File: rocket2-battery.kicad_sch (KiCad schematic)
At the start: 57 parts, among them J1 Conn_01x07, J2 SMA, J3 ARM Cortex Debug, P1 PAD_SMD, P2 PAD_SMD, P3 PAD_SMD, P4 PAD_SMD, P5 PAD_SMD, P6 PAD_SMD, Q1 NMOS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

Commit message: some minor fixes
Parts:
- added D17, D18: 30V 2A, Diode_SMD:D_0603_1608Metric_Pad1.05x0.95mm_HandSolder, symbol Device:D_Schottky
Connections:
- net +24V: now also D18.2 (A)
- net BATT_MAIN+: now also D17.2 (A); no longer C1.1, U1.1 (IN)
- new net: C1.1, D17.1 (K), D18.1 (K), U1.1 (IN)
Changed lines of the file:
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@@
   (junction (at 252.73 123.19) (diameter 0) (color 0 0 0 0)
   )
-  (junction (at 142.24 158.75) (diameter 0) (color 0 0 0 0)
-  )
   (junction (at 168.91 123.19) (diameter 0) (color 0 0 0 0)
   )
@@
   (junction (at 187.96 25.4) (diameter 0) (color 0 0 0 0)
   )
+  (junction (at 142.24 158.75) (diameter 0) (color 0 0 0 0)
+  )
   (junction (at 241.3 44.45) (diameter 0) (color 0 0 0 0)
   )
@@
   (junction (at 86.36 92.71) (diameter 0) (color 0 0 0 0)
   )
+  (junction (at 142.24 153.67) (diameter 0) (color 0 0 0 0)
+  )
   (junction (at 74.93 115.57) (diameter 0) (color 0 0 0 0)
   )
@@
     (stroke (width 0) (type default))
   )
+  (wire (pts (xy 153.67 149.86) (xy 151.13 149.86))
+    (stroke (width 0) (type default))
+  )
   (wire (pts (xy 151.13 129.54) (xy 151.13 132.08))
     (stroke (width 0) (type default))
@@
     (stroke (width 0) (type default))
   )
+  (wire (pts (xy 142.24 153.67) (xy 146.05 153.67))
+    (stroke (width 0) (type default))
+  )
   (wire (pts (xy 185.42 95.25) (xy 185.42 96.52))
     (stroke (width 0) (type default))
@@
     (stroke (width 0) (type default))
   )
+  (wire (pts (xy 142.24 149.86) (xy 142.24 153.67))
+    (stroke (width 0) (type default))
+  )
   (wire (pts (xy 185.42 25.4) (xy 187.96 25.4))
     (stroke (width 0) (type default))
@@
     (stroke (width 0) (type default))
   )
+  (wire (pts (xy 143.51 149.86) (xy 142.24 149.86))
+    (stroke (width 0) (type default))
+  )
   (wire (pts (xy 241.3 44.45) (xy 241.3 49.53))
     (stroke (width 0) (type default))
@@
     (stroke (width 0) (type default))
   )
+  (wire (pts (xy 142.24 153.67) (xy 142.24 158.75))
+    (stroke (width 0) (type default))
+  )
   (wire (pts (xy 31.75 60.96) (xy 31.75 83.82))
     (stroke (width 0) (type default))
@@
     (stroke (width 0) (type default))
   )
-  (wire (pts (xy 135.89 158.75) (xy 142.24 158.75))
-    (stroke (width 0) (type default))
-  )
   (wire (pts (xy 200.66 156.21) (xy 203.2 156.21))
     (stroke (width 0) (type default))
@@
     (stroke (width 0) (type default))
   )
+  (wire (pts (xy 156.21 153.67) (xy 153.67 153.67))
+    (stroke (width 0) (type default))
+  )
   (wire (pts (xy 184.15 123.19) (xy 184.15 124.46))
     (stroke (width 0) (type default))
@@
     (effects (font (size 1.27 1.27)) (justify left bottom))
   )
-  (label "BATT_MAIN+" (at 135.89 158.75 0) (fields_autoplaced)
+  (label "BATT_MAIN+" (at 156.21 153.67 0) (fields_autoplaced)
     (effects (font (size 1.27 1.27)) (justify left bottom))
   )
@@
   )
   (symbol (lib_id "UCIRP-KiCAD-Lib:NCV8730") (at 157.48 161.29 0) (unit 1)
-    (in_bom yes) (on_board yes) (dnp no) (fields_autoplaced)
-    (property "Reference" "U1" (at 157.47 149.86 0)
+    (in_bom yes) (on_board yes) (dnp no)
+    (property "Reference" "U1" (at 157.48 158.75 0)
       (effects (font (size 1.27 1.27)))
     )
@@
     )
   )
+  (symbol (lib_id "power:+24V") (at 153.67 149.86 270) (unit 1)
+    (in_bom yes) (on_board yes) (dnp no) (fields_autoplaced)
+    (property "Reference" "#PWR045" (at 149.86 149.86 0)
+      (effects (font (size 1.27 1.27)) hide)
+    )
+    (property "Value" "+24V" (at 157.48 150.495 90)
+      (effects (font (size 1.27 1.27)) (justify left))
+    )
+    (property "Footprint" "" (at 153.67 149.86 0)
+      (effects (font (size 1.27 1.27)) hide)
+    )
+    (property "Datasheet" "" (at 153.67 149.86 0)
+      (effects (font (size 1.27 1.27)) hide)
+    )
+    (pin "1")
+    (instances
+      (project "rocket2-battery"
+        (path "/453543af-7e3c-49a0-a644-4bd49c4f86f8"
+          (reference "#PWR045") (unit 1)
+        )
+      )
+    )
+  )
   (symbol (lib_id "power:GND") (at 182.88 97.79 0) (unit 1)
     (in_bom yes) (on_board yes) (dnp no)
@@
     )
   )
+  (symbol (lib_id "Device:D_Schottky") (at 147.32 149.86 0) (unit 1)
+    (in_bom yes) (on_board yes) (dnp no)
+    (property "Reference" "D18" (at 137.16 151.13 90)
+      (effects (font (size 1.27 1.27)))
+    )
+    (property "Value" "30V 2A" (at 137.16 157.48 90)
+      (effects (font (size 1.27 1.27)))
+    )
+    (property "Footprint" "Diode_SMD:D_0603_1608Metric_Pad1.05x0.95mm_HandSolder" (at 147.32 149.86 0)
+      (effects (font (size 1.27 1.27)) hide)
+    )
+    (property "Datasheet" "https://www.mouser.com/datasheet/2/308/1/NSR20F30_D-2318285.pdf" (at 147.32 149.86 0)
+      (effects (font (size 1.27 1.27)) hide)
+    )
+    (property "Manufacturer" "Onsemi" (at 147.32 149.86 0)
+      (effects (font (size 1.27 1.27)) hide)
+    )
+    (property "Part #" "NSR20F30NXT5G" (at 147.32 149.86 0)
+      (effects (font (size 1.27 1.27)) hide)
+    )
+    (pin "1")
+    (pin "2")
+    (instances
+      (project "rocket2-battery"
+        (path "/453543af-7e3c-49a0-a644-4bd49c4f86f8"
+          (reference "D18") (unit 1)
+        )
+      )
+    )
+  )
   (symbol (lib_id "power:+3.3V") (at 210.82 20.32 0) (unit 1)
     (in_bom yes) (on_board yes) (dnp no)
@@
         )
       )
+    )
+  )
+  (symbol (lib_id "Device:D_Schottky") (at 149.86 153.67 0) (unit 1)
+    (in_bom yes) (on_board yes) (dnp no)
+    (property "Reference" "D17" (at 139.7 160.02 90)
+      (effects (font (size 1.27 1.27)))
+    )
+    (property "Value" "30V 2A" (at 139.7 153.67 90)
+      (effects (font (size 1.27 1.27)))
+    )
+    (property "Footprint" "Diode_SMD:D_0603_1608Metric_Pad1.05x0.95mm_HandSolder" (at 149.86 153.67 0)
+      (effects (font (size 1.27 1.27)) hide)
+    )
+    (property "Datasheet" "https://www.mouser.com/datasheet/2/308/1/NSR20F30_D-2318285.pdf" (at 149.86 153.67 0)
+      (effects (font (size 1.27 1.27)) hide)
+    )
+    (property "Manufacturer" "Onsemi" (at 149.86 153.67 0)
+      (effects (font (size 1.27 1.27)) hide)
+    )
+    (property "Part #" "NSR20F30NXT5G" (at 149.86 153.67 0)
+      (effects (font (size 1.27 1.27)) hide)
+    )
+    (pin "1")
+    (pin "2")
+    (instances
+      (project "rocket2-battery"
+        (path "/453543af-7e3c-49a0-a644-4bd49c4f86f8"
+          (reference "D17") (unit 1)
+        )
+      )

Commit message: Fix diode footprints & other things I don't remember
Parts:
- D17, D18, D2, D4: footprint Diode_SMD:D_0603_1608Metric_Pad1.05x0.95mm_HandSolder -> Diode_SMD:Nexperia_DSN1608-2_1.6x0.8mm
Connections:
- net +24V: now also D18.1 (A); no longer D18.2 (A)
- net BATT_MAIN+: now also D17.1 (A); no longer D17.2 (A)
- net MAIN+: now also D2.2 (K), D4.2 (K); no longer D2.1 (K), D4.1 (K)
- net at C1.1, U1.1 (IN): now also D17.2 (K), D18.2 (K); no longer D17.1 (K), D18.1 (K)
- net at Q7.5 (D), Q8.5 (D): now also D4.1 (A); no longer D4.2 (A)
- net at Q3.5 (D), Q4.5 (D): now also D2.1 (A); no longer D2.2 (A)
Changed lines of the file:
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@@
       (effects (font (size 1.27 1.27)))
     )
-    (property "Footprint" "Diode_SMD:D_0603_1608Metric_Pad1.05x0.95mm_HandSolder" (at 262.89 123.19 0)
+    (property "Footprint" "Diode_SMD:Nexperia_DSN1608-2_1.6x0.8mm" (at 262.89 123.19 0)
       (effects (font (size 1.27 1.27)) hide)
     )
@@
     )
   )
-  (symbol (lib_id "Device:D_Schottky") (at 147.32 149.86 0) (unit 1)
+  (symbol (lib_name "D_Schottky_1") (lib_id "Device:D_Schottky") (at 147.32 149.86 0) (unit 1)
     (in_bom yes) (on_board yes) (dnp no)
     (property "Reference" "D18" (at 137.16 151.13 90)
@@
       (effects (font (size 1.27 1.27)))
     )
-    (property "Footprint" "Diode_SMD:D_0603_1608Metric_Pad1.05x0.95mm_HandSolder" (at 147.32 149.86 0)
+    (property "Footprint" "Diode_SMD:Nexperia_DSN1608-2_1.6x0.8mm" (at 147.32 149.86 0)
       (effects (font (size 1.27 1.27)) hide)
     )
@@
     )
   )
-  (symbol (lib_id "Device:D_Schottky") (at 149.86 153.67 0) (unit 1)
+  (symbol (lib_name "D_Schottky_2") (lib_id "Device:D_Schottky") (at 149.86 153.67 0) (unit 1)
     (in_bom yes) (on_board yes) (dnp no)
     (property "Reference" "D17" (at 139.7 160.02 90)
@@
       (effects (font (size 1.27 1.27)))
     )
-    (property "Footprint" "Diode_SMD:D_0603_1608Metric_Pad1.05x0.95mm_HandSolder" (at 149.86 153.67 0)
+    (property "Footprint" "Diode_SMD:Nexperia_DSN1608-2_1.6x0.8mm" (at 149.86 153.67 0)
       (effects (font (size 1.27 1.27)) hide)
     )
@@
     )
   )
-  (symbol (lib_id "Device:D_Schottky") (at 194.31 123.19 180) (unit 1)
+  (symbol (lib_name "D_Schottky_3") (lib_id "Device:D_Schottky") (at 194.31 123.19 180) (unit 1)
     (in_bom yes) (on_board yes) (dnp no)
     (property "Reference" "D2" (at 194.6275 118.11 0)
@@
       (effects (font (size 1.27 1.27)))
     )
-    (property "Footprint" "Diode_SMD:D_0603_1608Metric_Pad1.05x0.95mm_HandSolder" (at 194.31 123.19 0)
-      (effects (font (size 1.27 1.27)) hide)
-    )
+    (property "Footprint" "Diode_SMD:Nexperia_DSN1608-2_1.6x0.8mm" (at 194.31 123.19 0)
+      (effects (font (size 1.27 1.27)) hide)
+    )

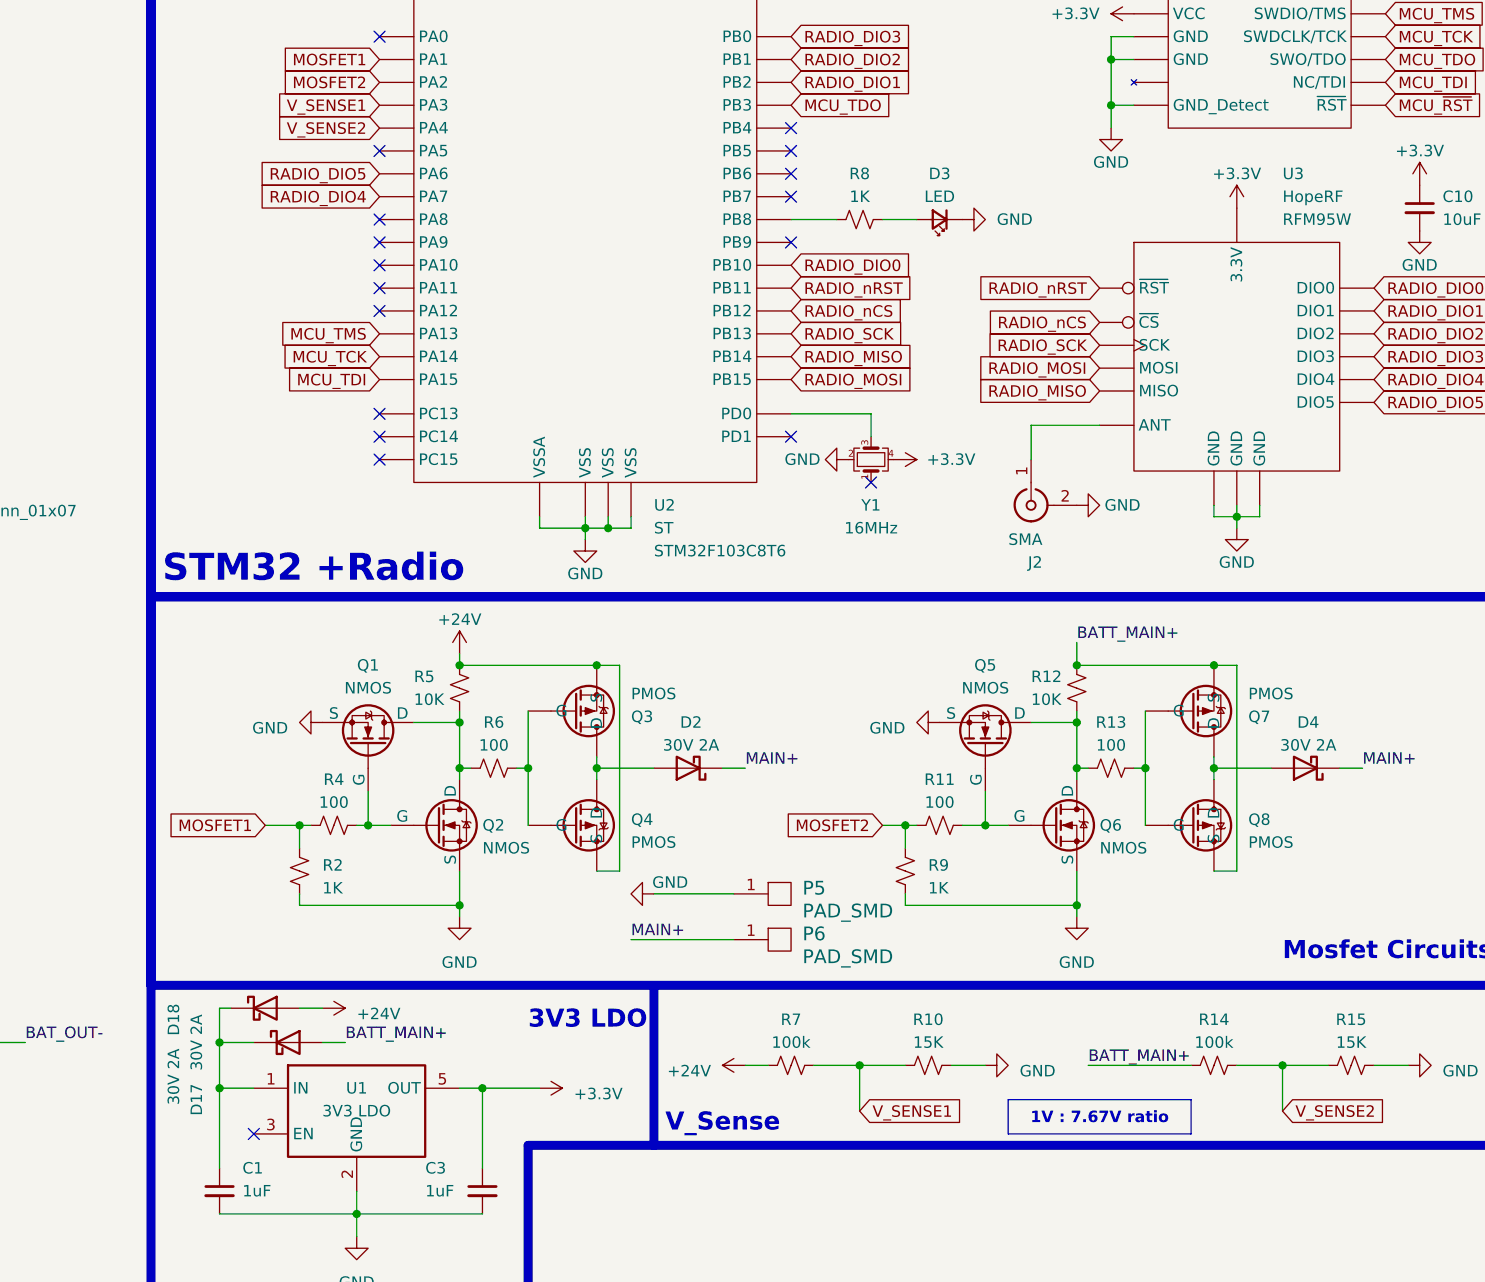
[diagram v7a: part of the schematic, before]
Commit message: fixed nmos
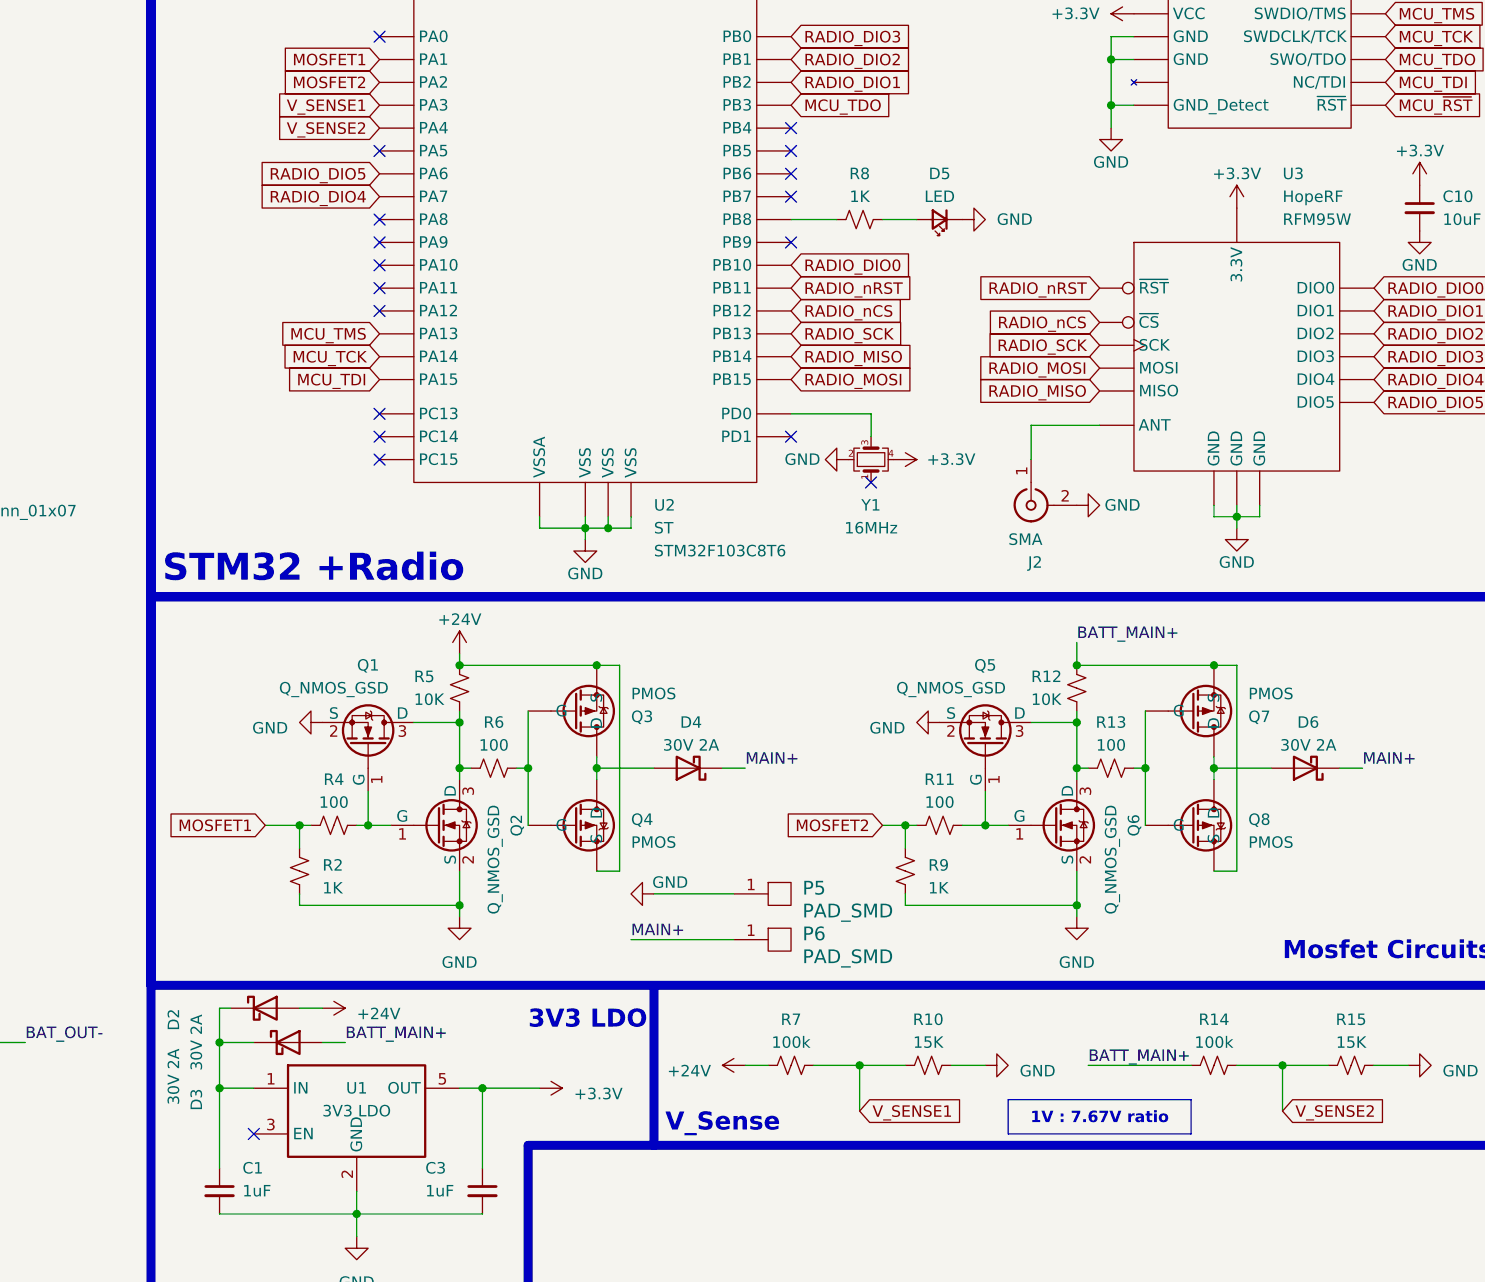
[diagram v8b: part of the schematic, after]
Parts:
- removed Q1, Q2, Q5, Q6: NMOS, Package_TO_SOT_SMD:SOT-23-3, symbol Simulation_SPICE:NMOS
- added Q1, Q2, Q5, Q6: Q_NMOS_GSD, Package_TO_SOT_SMD:SOT-23-3, symbol Device:Q_NMOS_GSD
- renumbered D18 to D2, D17 to D3, D2 to D4, D3 to D5, D4 to D6
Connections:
- net GND: now also Q1.2 (S), Q2.2 (S), Q5.2 (S), Q6.2 (S)
- net at R12.2, R13.1: now also Q5.3 (D), Q6.3 (D)
- net at R11.2: now also Q5.1 (G), Q6.1 (G)
- net at R5.2, R6.1: now also Q1.3 (D), Q2.3 (D)
- net at R4.2: now also Q1.1 (G), Q2.1 (G)
